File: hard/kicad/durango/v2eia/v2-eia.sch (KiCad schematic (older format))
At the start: 50 parts, among them J1 NANOLINK, J10 STEP, J2 AUDIO IN, J3 IOx, Q1 BC548, Q2 BC548, Q3 BC548, Q307 BC548, U1 65C02, U10 74HC139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

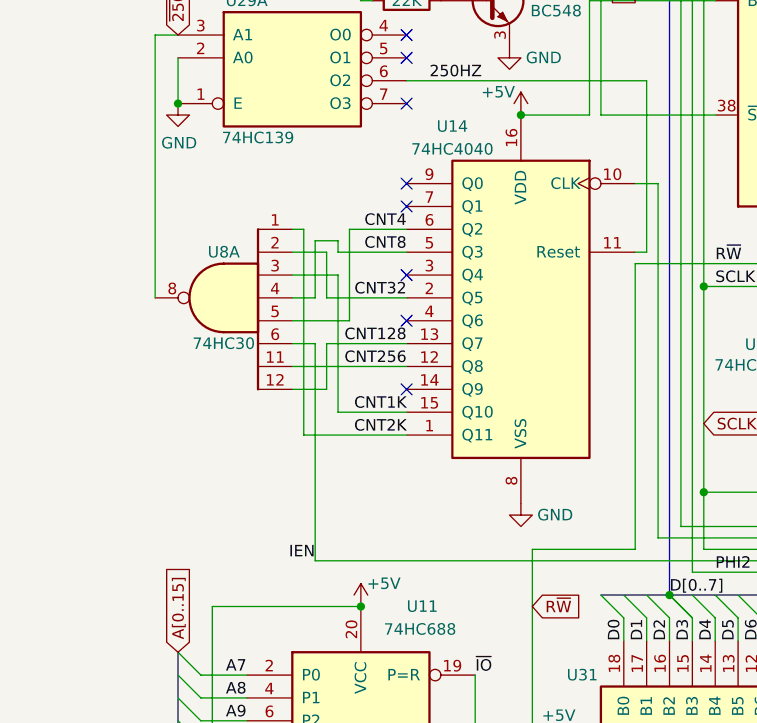
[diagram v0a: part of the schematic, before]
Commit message: fix interrupt rate on EIA
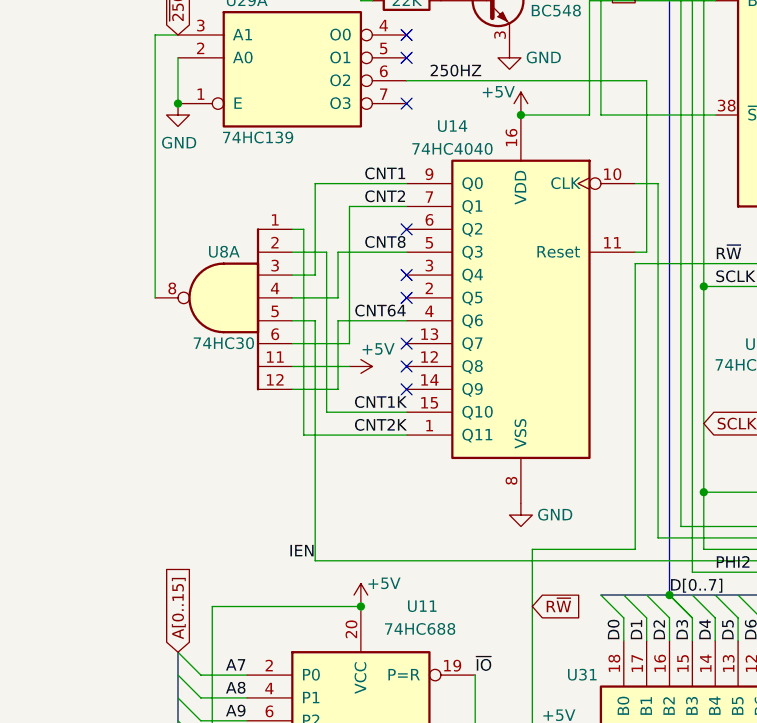
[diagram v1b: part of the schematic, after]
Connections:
- net +5V: now also U8.11
- net CNT1K: now also U8.2; no longer U8.3
- net MA[0..14]: now also U8.5; no longer U8.6
- net CNT64: now reaches U14.4 (Q6)
- net CNT64: now also U8.12
- net CNT2: now reaches U14.7 (Q1)
- net CNT2: now also U8.6
- net CNT1: now reaches U14.9 (Q0)
- net CNT1: now also U8.3
- net CNT128: no longer names the net of U14.13 (Q7)
- net CNT128: no longer U8.12
- net CNT256: no longer names the net of U14.12 (Q8)
- net CNT256: no longer U8.11
- net CNT32: no longer names the net of U14.2 (Q5)
- net CNT32: no longer U8.2
- net CNT4: no longer names the net of U14.6 (Q2)
- net CNT4: no longer U8.5
- no-connect marks 14 -> 15
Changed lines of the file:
@@
 Wire Wire Line
 	550  2800 550  3950
-NoConn ~ 1650 3450
-NoConn ~ 1650 3550
-NoConn ~ 1650 3850
-NoConn ~ 1650 4050
+NoConn ~ 1650 3950
 NoConn ~ 1650 4350
-Text Label 1650 3650 2    50   ~ 0
-CNT4
+Text Label 1650 3450 2    50   ~ 0
+CNT1
+Text Label 1650 3550 2    50   ~ 0
+CNT2
 Text Label 1650 3750 2    50   ~ 0
 CNT8
-Text Label 1650 3950 2    50   ~ 0
-CNT32
-Text Label 1650 4150 2    50   ~ 0
-CNT128
-Text Label 1650 4250 2    50   ~ 0
-CNT256
+Text Label 1650 4050 2    50   ~ 0
+CNT64
 Text Label 1650 4450 2    50   ~ 0
 CNT1K
@@
 	1200 4550 1650 4550
 Wire Wire Line
-	1150 3750 1300 3750
-Wire Wire Line
-	1300 3750 1300 3950
-Wire Wire Line
-	1300 3950 1650 3950
-Wire Wire Line
-	1150 3850 1350 3850
-Wire Wire Line
-	1350 3850 1350 4450
-Wire Wire Line
-	1350 4450 1650 4450
-Wire Wire Line
-	1150 3950 1250 3950
-Wire Wire Line
-	1250 3950 1250 3700
-Wire Wire Line
-	1250 3700 1350 3700
-Wire Wire Line
-	1350 3700 1350 3750
-Wire Wire Line
-	1350 3750 1650 3750
-Wire Wire Line
-	1150 4050 1400 4050
-Wire Wire Line
-	1400 4050 1400 3650
-Wire Wire Line
-	1400 3650 1650 3650
-Wire Wire Line
-	1150 4150 1250 4150
-Wire Wire Line
-	1250 4150 1250 5100
-Wire Wire Line
 	1250 5100 5750 5100
-Wire Wire Line
-	1150 4350 1300 4350
-Wire Wire Line
-	1300 4350 1300 4150
-Wire Wire Line
-	1300 4150 1650 4150
-Wire Wire Line
-	1150 4250 1650 4250
 $Comp
 L Diode:1N4148 D8
@@
 Text GLabel 9400 3600 2    50   Input ~ 0
 ~DWE
+NoConn ~ 1650 3650
+NoConn ~ 1650 3850
+NoConn ~ 1650 4150
+NoConn ~ 1650 4250
+Wire Wire Line
+	1150 3750 1300 3750
+Wire Wire Line
+	1300 3750 1300 4450
+Wire Wire Line
+	1300 4450 1650 4450
+Wire Wire Line
+	1650 3750 1350 3750
+Wire Wire Line
+	1350 3750 1350 3950
+Wire Wire Line
+	1350 3950 1150 3950
+Wire Wire Line
+	1250 4050 1150 4050
+Wire Wire Line
+	1250 4050 1250 5100
+Wire Wire Line
+	1150 4350 1350 4350
+Wire Wire Line
+	1350 4350 1350 4050
+Wire Wire Line
+	1350 4050 1650 4050
+Wire Wire Line
+	1150 4250 1400 4250
+$Comp
+L power:+5V #PWR?
+U 1 1 65DD1D3F
+P 1400 4250
+F 0 "#PWR?" H 1400 4100 50  0001 C CNN
+F 1 "+5V" V 1325 4300 50  0000 L CNN
+F 2 "" H 1400 4250 50  0001 C CNN
+F 3 "" H 1400 4250 50  0001 C CNN
+	1    1400 4250
+	0    1    1    0
+$EndComp
+Wire Wire Line
+	1150 4150 1400 4150
+Wire Wire Line
+	1400 4150 1400 3550
+Wire Wire Line
+	1400 3550 1650 3550
+Wire Wire Line
+	1150 3850 1250 3850
+Wire Wire Line
+	1250 3850 1250 3450
+Wire Wire Line
+	1250 3450 1650 3450
 Wire Bus Line
 	2500 5250 2800 5250
